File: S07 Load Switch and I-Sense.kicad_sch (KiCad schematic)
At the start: 62 parts, among them Q20 DMN65D8LFB-7, Q21 DMN65D8LFB-7, Q22 DMN65D8LFB-7, U10 TLV9002IDSG, U6 TPS22811, U7 TPS22811, U8 TLV9002IDSG, U9 TPS22811

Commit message: Add a PCAL9714 SPI I/O expander for the load-switch enables and faults
New sheet S08 with U11 (PCAL9714, HVQFN-24) on the shared CLOCK/MOSI/MISO
bus. J3.32, which was ENSBC, becomes its chip select nCSIO.

- P0_0-P0_2 drive ENDAQ, ENSBC and ENEXT. J3.34/J3.36 become MCU_ENDAQ
  and MCU_ENEXT, and each reaches its enable only through a DNP 0R link
  (R96-R98). R95 links nCSIO to the expander CS.
- P0_4-P0_6 read the U6/U7/U9 power-good signals, and P0_7 reads U5
  nFLT/nINT.
- REGEN stays a direct J3.12 signal.
- RESET is divided from +12V (R99 100K, R100 40.2K), so the expander
  stays in reset while the 12 V rail is off.
- Pull-ups on CS and INT (R93, R94) and decoupling (C58, C59).

The README gains the port map, the links and the board work. The board
still needs Update PCB from Schematic.

Co-Authored-By: Claude Opus 5.5 <noreply@anthropic.com>
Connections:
- net PGEXT: now reaches Q22.1 (G), R78.1, U9.3 (PG)
- net PGSBC: now reaches Q21.1 (G), R65.1, U7.3 (PG)
- net PGDAQ: now reaches Q20.1 (G), R63.1, U6.3 (PG)
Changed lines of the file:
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@@
+	)
+	(junction
+		(at 134.62 196.85)
+		(diameter 0)
+		(color 0 0 0 0)
 	)
 	(junction
@@
 	)
 	(junction
+		(at 306.07 68.58)
+		(diameter 0)
+		(color 0 0 0 0)
+	)
+	(junction
 		(at 100.33 262.89)
+		(diameter 0)
+		(color 0 0 0 0)
+	)
+	(junction
+		(at 137.16 69.85)
 		(diameter 0)
 		(color 0 0 0 0)
@@
 		)
 	)
+	(wire
+		(pts
+			(xy 134.62 196.85) (xy 134.62 199.39)
+		)
+		(stroke
+			(width 0)
+			(type default)
+		)
+	)
 	(polyline
 		(pts
@@
 		)
 	)
+	(wire
+		(pts
+			(xy 306.07 68.58) (xy 306.07 71.12)
+		)
+		(stroke
+			(width 0)
+			(type default)
+		)
+	)
 	(polyline
 		(pts
@@
 		(pts
 			(xy 124.46 69.85) (xy 144.78 69.85)
+		)
+		(stroke
+			(width 0)
+			(type default)
+		)
+	)
+	(wire
+		(pts
+			(xy 137.16 69.85) (xy 137.16 72.39)
 		)
 		(stroke
@@
 		)
 	)
+	(hierarchical_label "PGSBC"
+		(shape output)
+		(at 137.16 72.39 270)
+		(effects
+			(font
+				(size 1.27 1.27)
+			)
+			(justify right)
+		)
+	)
 	(hierarchical_label "OUTEXT"
 		(shape passive)
@@
 		)
 	)
+	(hierarchical_label "PGDAQ"
+		(shape output)
+		(at 134.62 199.39 270)
+		(effects
+			(font
+				(size 1.27 1.27)
+			)
+			(justify right)
+		)
+	)
 	(hierarchical_label "IAMPSBC"
 		(shape passive)
@@
 	)
 	(hierarchical_label "ENDAQ"
-		(shape passive)
+		(shape input)
 		(at 38.1 185.42 180)
+		(effects
+			(font
+				(size 1.27 1.27)
+			)
+			(justify right)
+		)
+	)
+	(hierarchical_label "PGEXT"
+		(shape output)
+		(at 306.07 71.12 270)
 		(effects
 			(font
@@
 	)
 	(hierarchical_label "ENEXT"
-		(shape passive)
+		(shape input)
 		(at 209.55 57.15 180)
 		(effects
@@
 	)
 	(hierarchical_label "ENSBC"
-		(shape passive)
+		(shape input)
 		(at 40.64 58.42 180)
 		(effects

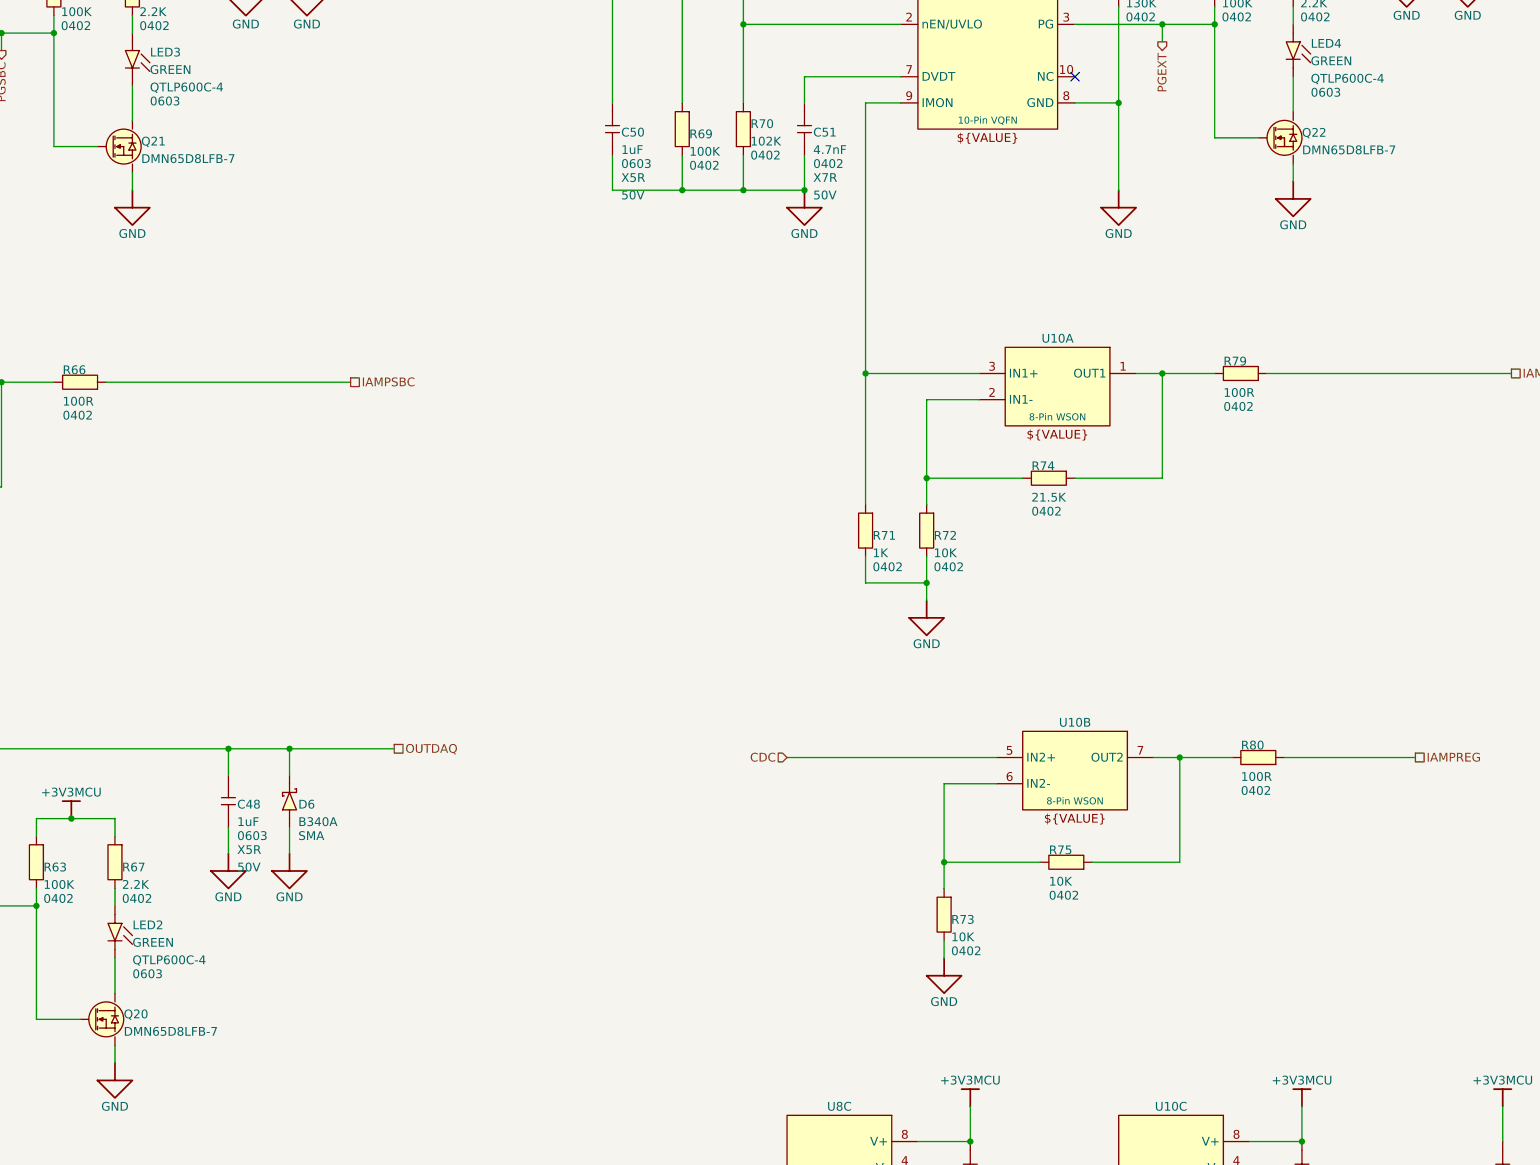
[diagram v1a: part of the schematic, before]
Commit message: Drive the expander RESET through a FET and use BSS138 for Q20-Q23
The +12V divider on U11 RESET could back-power the expander and gave a
weak logic high. Q23 now passes +3V3MCU to RESET while +12V is up, with
its gate fed by R99 100K / R101 1M. R100 (now 100K) holds RESET low when
+12V is off, and RESET can no longer rise above +3V3MCU.

Q20-Q23 are now onsemi BSS138 in SOT-23, replacing the DFN1006
DMN65D8LFB-7. The BSS138 has no gate zener, so gate leakage is at most
100 nA on the 100K PG pull-ups and the Q23 gate divider. The README
warns against ESD-protected substitutes.

The root sheet change is KiCad reordering items only.

Co-Authored-By: Claude Opus 5.5 <noreply@anthropic.com>
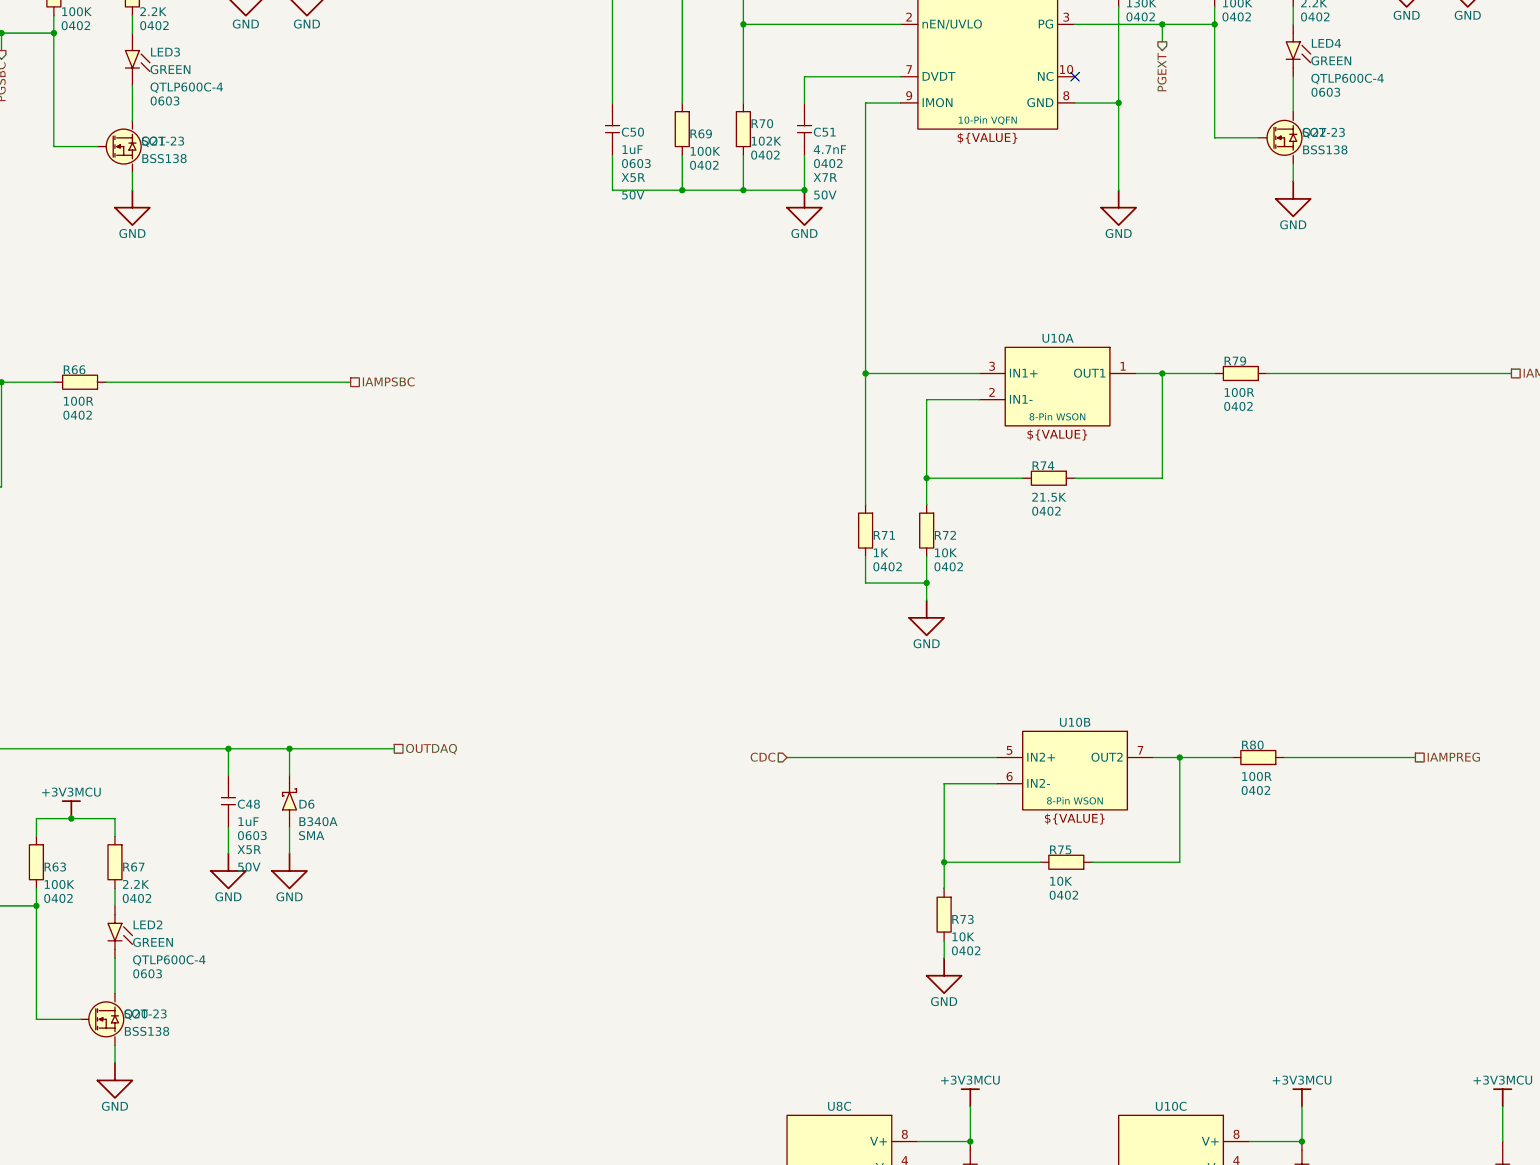
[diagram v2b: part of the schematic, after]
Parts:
- Q20, Q21, Q22: value DMN65D8LFB-7 -> BSS138; footprint EVO2513-0_5_0-import-fps:FET 3-Pin DFN1006 -> Package_TO_SOT_SMD:SOT-23; symbol Lattech Systems:Transistor N-Channel MOSFET 60V DMN65D8LFB-7 -> Lattech Systems:Transistor N-Channel MOSFET 50V BSS138 SOT-23; ALTIUM_FOOTPRINT (none) -> SOT-23; ALTIUM_VALUE DMN65D8LFB-7 -> BSS138; MANUFACTURER Diodes Inc -> onsemi; MANUFACTURER_PN DMN65D8LFB-7 -> BSS138
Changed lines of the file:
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@@
 	)
 	(symbol
-		(lib_id "Lattech Systems:Transistor N-Channel MOSFET 60V DMN65D8LFB-7")
+		(lib_id "Lattech Systems:Transistor N-Channel MOSFET 50V BSS138 SOT-23")
 		(at 323.85 85.09 0)
 		(unit 1)
@@
 			)
 		)
-		(property "Value" "DMN65D8LFB-7"
+		(property "Value" "BSS138"
 			(at 323.85 85.09 0)
 			(hide yes)
@@
 			)
 		)
-		(property "Footprint" "EVO2513-0_5_0-import-fps:FET 3-Pin DFN1006"
+		(property "Footprint" "Package_TO_SOT_SMD:SOT-23"
 			(at 323.85 85.09 0)
 			(hide yes)
@@
 			)
 		)
-		(property "Description" "Transistor N-Channel MOSFET 60V DMN65D8LFB-7"
+		(property "Description" "Transistor N-Channel MOSFET 50V BSS138 SOT-23"
 			(at 323.85 85.09 0)
 			(hide yes)
@@
 			)
 		)
-		(property "MANUFACTURER" "Diodes Inc"
+		(property "MANUFACTURER" "onsemi"
 			(at 319.532 80.772 0)
 			(hide yes)
@@
 			)
 		)
-		(property "MANUFACTURER_PN" "DMN65D8LFB-7"
+		(property "MANUFACTURER_PN" "BSS138"
 			(at 319.532 80.772 0)
 			(hide yes)
@@
 			)
 		)
-		(property "ALTIUM_FOOTPRINT" ""
+		(property "ALTIUM_FOOTPRINT" "SOT-23"
 			(at 326.39 85.09 0)
 			(show_name no)
@@
 			)
 		)
-		(property "ALTIUM_VALUE" "DMN65D8LFB-7"
+		(property "ALTIUM_VALUE" "BSS138"
 			(at 326.39 87.63 0)
 			(show_name no)
@@
 	)
 	(symbol
-		(lib_id "Lattech Systems:Transistor N-Channel MOSFET 60V DMN65D8LFB-7")
+		(lib_id "Lattech Systems:Transistor N-Channel MOSFET 50V BSS138 SOT-23")
 		(at 154.94 86.36 0)
 		(unit 1)
@@
 			)
 		)
-		(property "Value" "DMN65D8LFB-7"
+		(property "Value" "BSS138"
 			(at 154.94 86.36 0)
 			(hide yes)
@@
 			)
 		)
-		(property "Footprint" "EVO2513-0_5_0-import-fps:FET 3-Pin DFN1006"
+		(property "Footprint" "Package_TO_SOT_SMD:SOT-23"
 			(at 154.94 86.36 0)
 			(hide yes)
@@
 			)
 		)
-		(property "Description" "Transistor N-Channel MOSFET 60V DMN65D8LFB-7"
+		(property "Description" "Transistor N-Channel MOSFET 50V BSS138 SOT-23"
 			(at 154.94 86.36 0)
 			(hide yes)
@@
 			)
 		)
-		(property "MANUFACTURER" "Diodes Inc"
+		(property "MANUFACTURER" "onsemi"
 			(at 150.622 82.042 0)
 			(hide yes)
@@
 			)
 		)
-		(property "MANUFACTURER_PN" "DMN65D8LFB-7"
+		(property "MANUFACTURER_PN" "BSS138"
 			(at 150.622 82.042 0)
 			(hide yes)
@@
 			)
 		)
-		(property "ALTIUM_FOOTPRINT" ""
+		(property "ALTIUM_FOOTPRINT" "SOT-23"
 			(at 157.48 86.36 0)
 			(show_name no)
@@
 			)
 		)
-		(property "ALTIUM_VALUE" "DMN65D8LFB-7"
+		(property "ALTIUM_VALUE" "BSS138"
 			(at 157.48 88.9 0)
 			(show_name no)
@@
 	)
 	(symbol
-		(lib_id "Lattech Systems:Transistor N-Channel MOSFET 60V DMN65D8LFB-7")
+		(lib_id "Lattech Systems:Transistor N-Channel MOSFET 50V BSS138 SOT-23")
 		(at 152.4 213.36 0)
 		(unit 1)
@@
 			)
 		)
-		(property "Value" "DMN65D8LFB-7"
+		(property "Value" "BSS138"
 			(at 152.4 213.36 0)
 			(hide yes)
@@
 			)
 		)
-		(property "Footprint" "EVO2513-0_5_0-import-fps:FET 3-Pin DFN1006"
+		(property "Footprint" "Package_TO_SOT_SMD:SOT-23"
 			(at 152.4 213.36 0)
 			(hide yes)
@@
 			)
 		)
-		(property "Description" "Transistor N-Channel MOSFET 60V DMN65D8LFB-7"
+		(property "Description" "Transistor N-Channel MOSFET 50V BSS138 SOT-23"
 			(at 152.4 213.36 0)
 			(hide yes)
@@
 			)
 		)
-		(property "MANUFACTURER" "Diodes Inc"
+		(property "MANUFACTURER" "onsemi"
 			(at 148.082 209.042 0)
 			(hide yes)
@@
 			)
 		)
-		(property "MANUFACTURER_PN" "DMN65D8LFB-7"
+		(property "MANUFACTURER_PN" "BSS138"
 			(at 148.082 209.042 0)
 			(hide yes)
@@
 			)
 		)
-		(property "ALTIUM_FOOTPRINT" ""
+		(property "ALTIUM_FOOTPRINT" "SOT-23"
 			(at 154.94 213.36 0)
 			(show_name no)
@@
 			)
 		)
-		(property "ALTIUM_VALUE" "DMN65D8LFB-7"
+		(property "ALTIUM_VALUE" "BSS138"
 			(at 154.94 215.9 0)
 			(show_name no)
